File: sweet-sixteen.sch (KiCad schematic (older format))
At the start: 8 parts

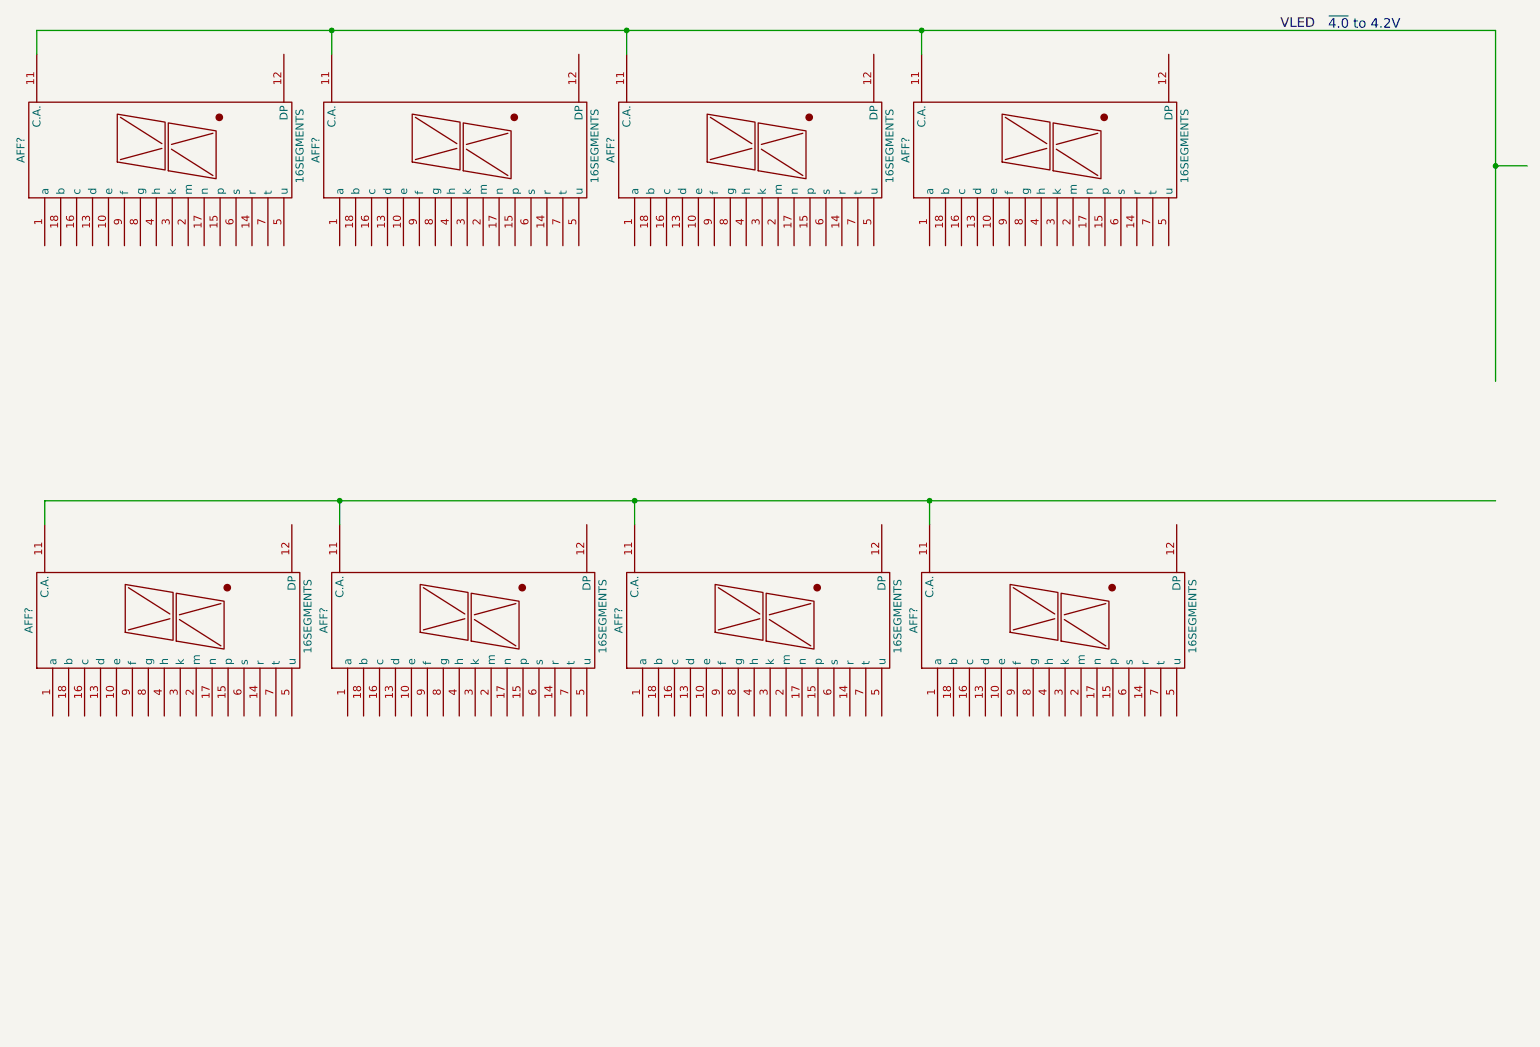
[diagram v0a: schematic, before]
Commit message: add led-drivers to schematic
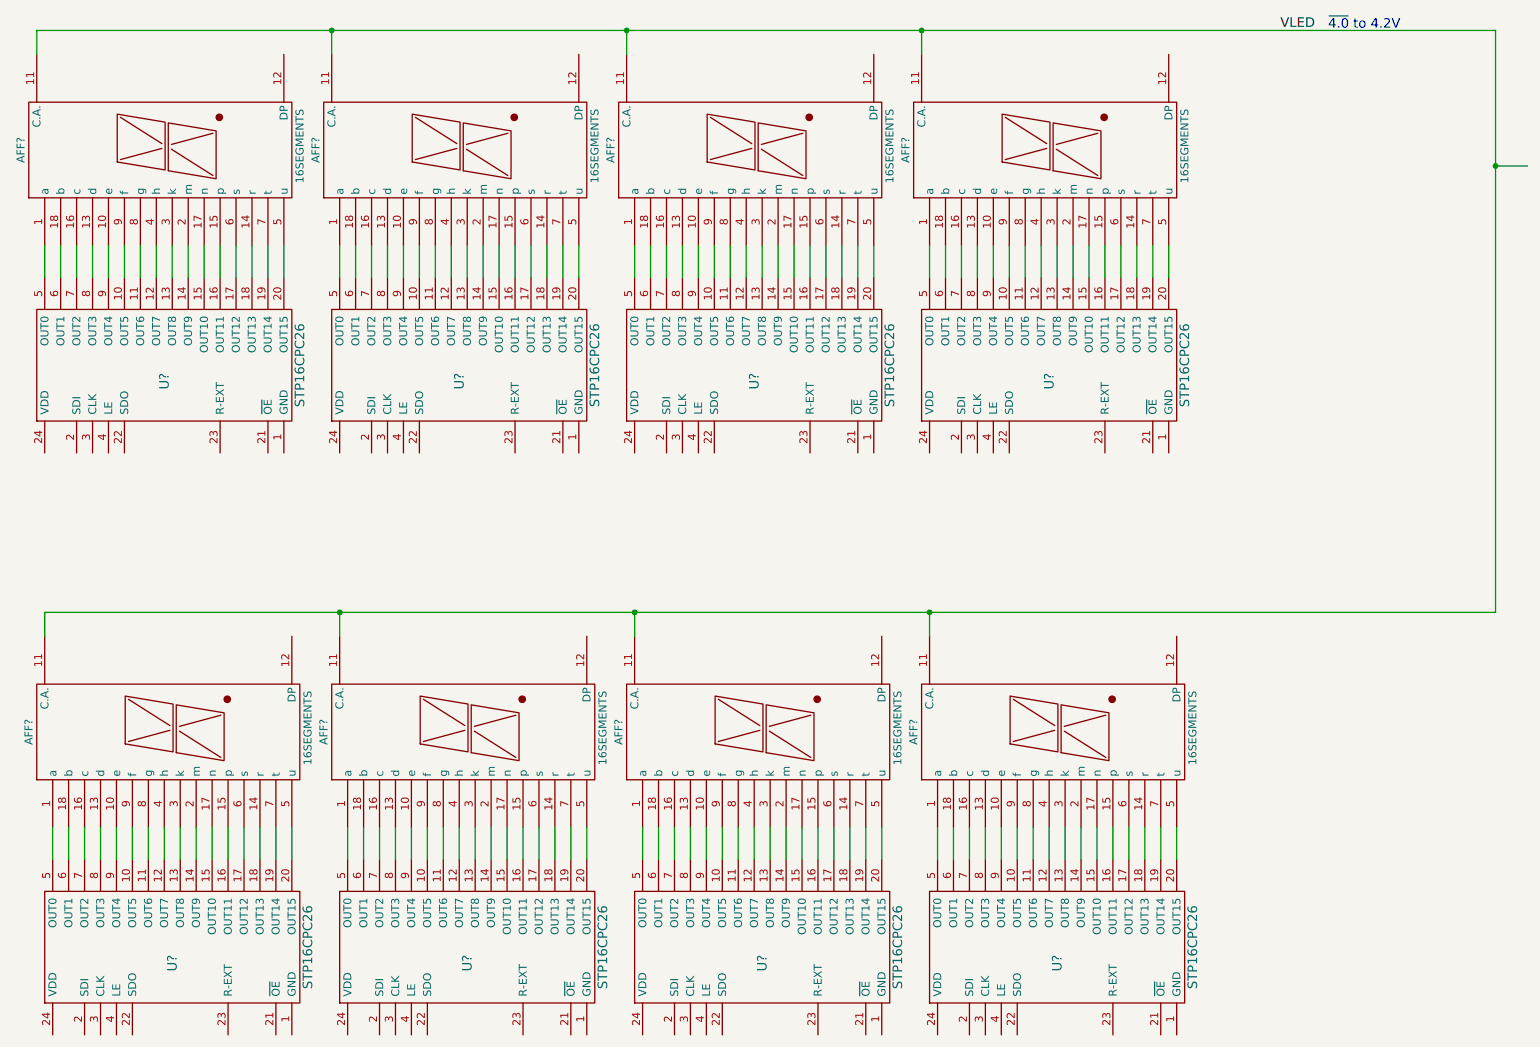
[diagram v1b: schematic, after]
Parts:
- added U? (x8): STP16CPC26, symbol STP16CPC26
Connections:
- wire segments 12 -> 140
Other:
- moved on the sheet: AFF?

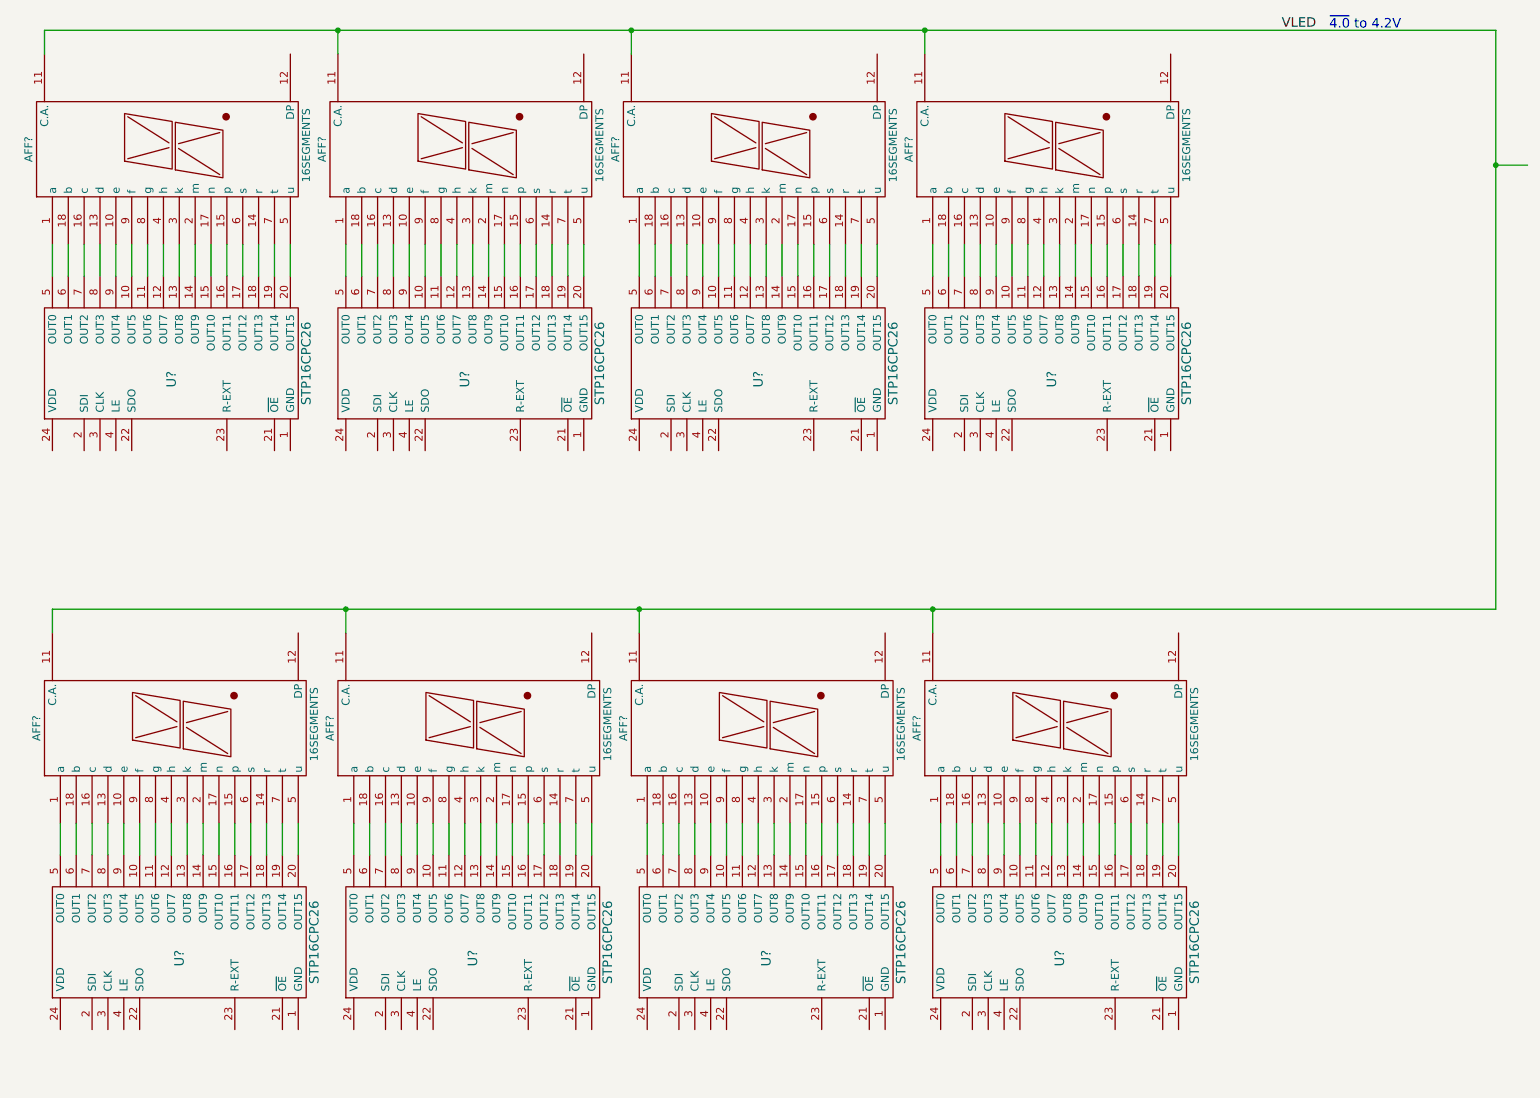
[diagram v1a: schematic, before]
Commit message: wire up displays and driver
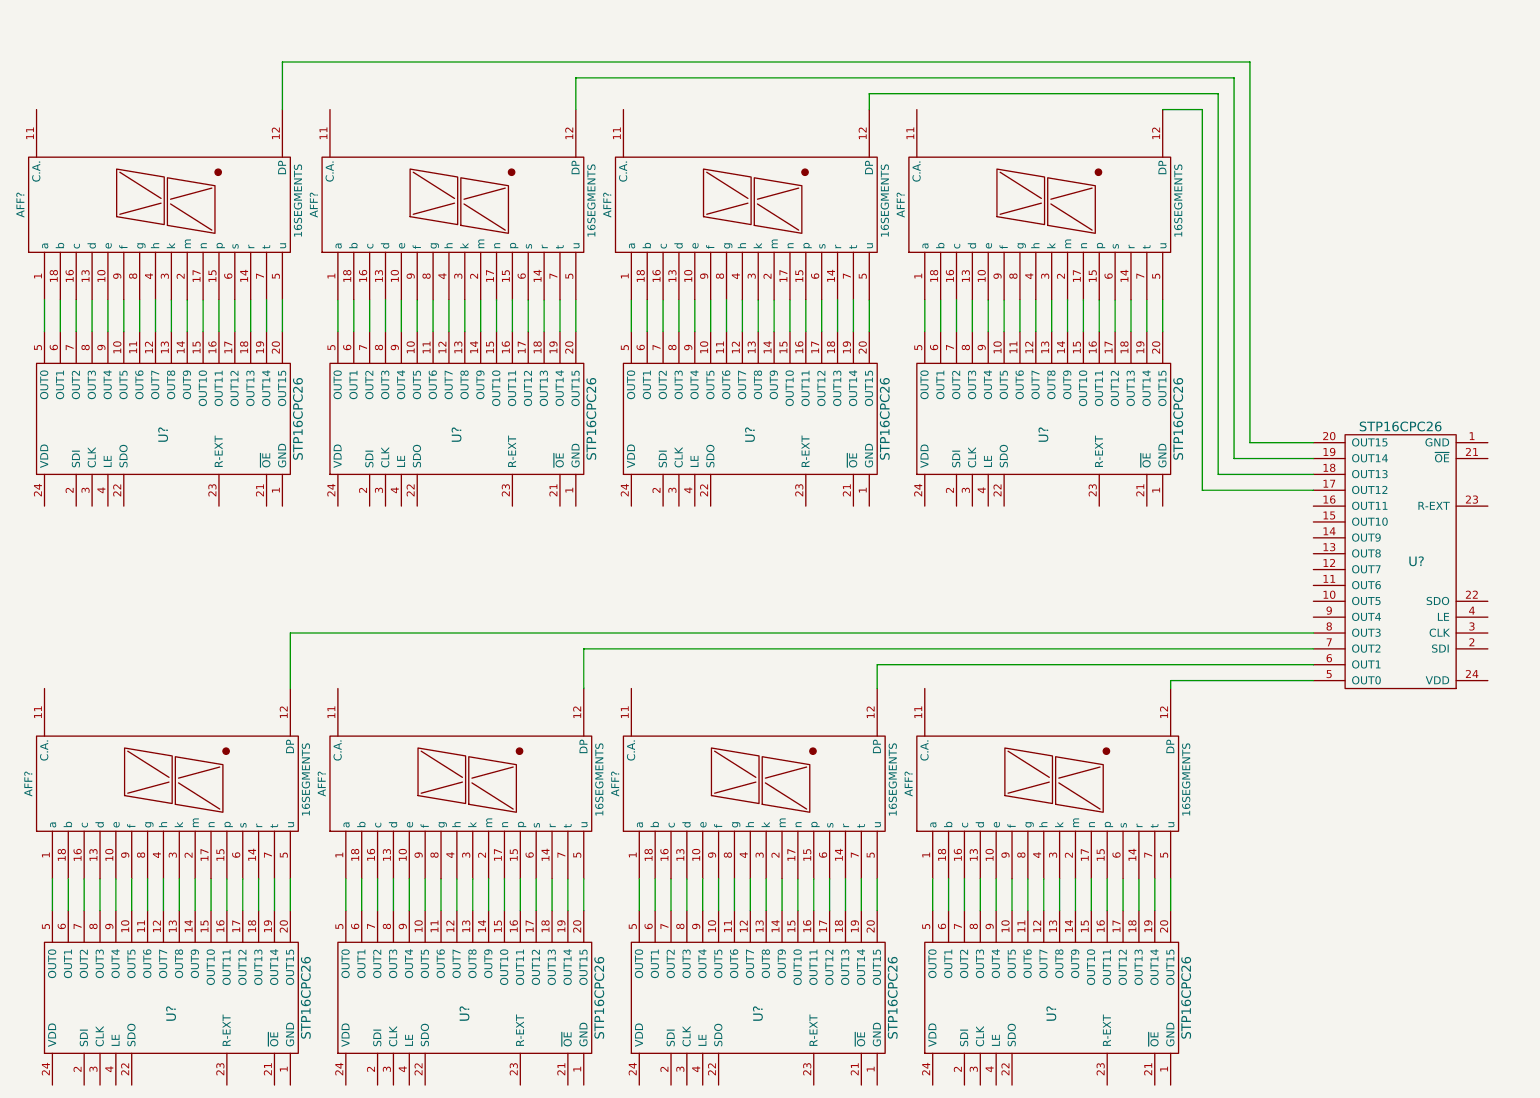
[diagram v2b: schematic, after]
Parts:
- added U?: STP16CPC26, symbol STP16CPC26
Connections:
- net at AFF?.12 (DP): now also U?.20 (OUT15)
- net at AFF?.12 (DP): now also U?.19 (OUT14)
- net at AFF?.12 (DP): now also U?.18 (OUT13)
- net at AFF?.12 (DP): now also U?.17 (OUT12)
- net at AFF?.12 (DP): now also U?.8 (OUT3)
- net at AFF?.12 (DP): now also U?.7 (OUT2)
- net at AFF?.12 (DP): now also U?.6 (OUT1)
- net at AFF?.12 (DP): now also U?.5 (OUT0)
- removed net VLED: AFF?.11 (C.A.), AFF?.11 (C.A.), AFF?.11 (C.A.), AFF?.11 (C.A.), AFF?.11 (C.A.), AFF?.11 (C.A.), AFF?.11 (C.A.), AFF?.11 (C.A.)
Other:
- note removed: "~4.0 to 4.2V"
- moved on the sheet: AFF?, U?

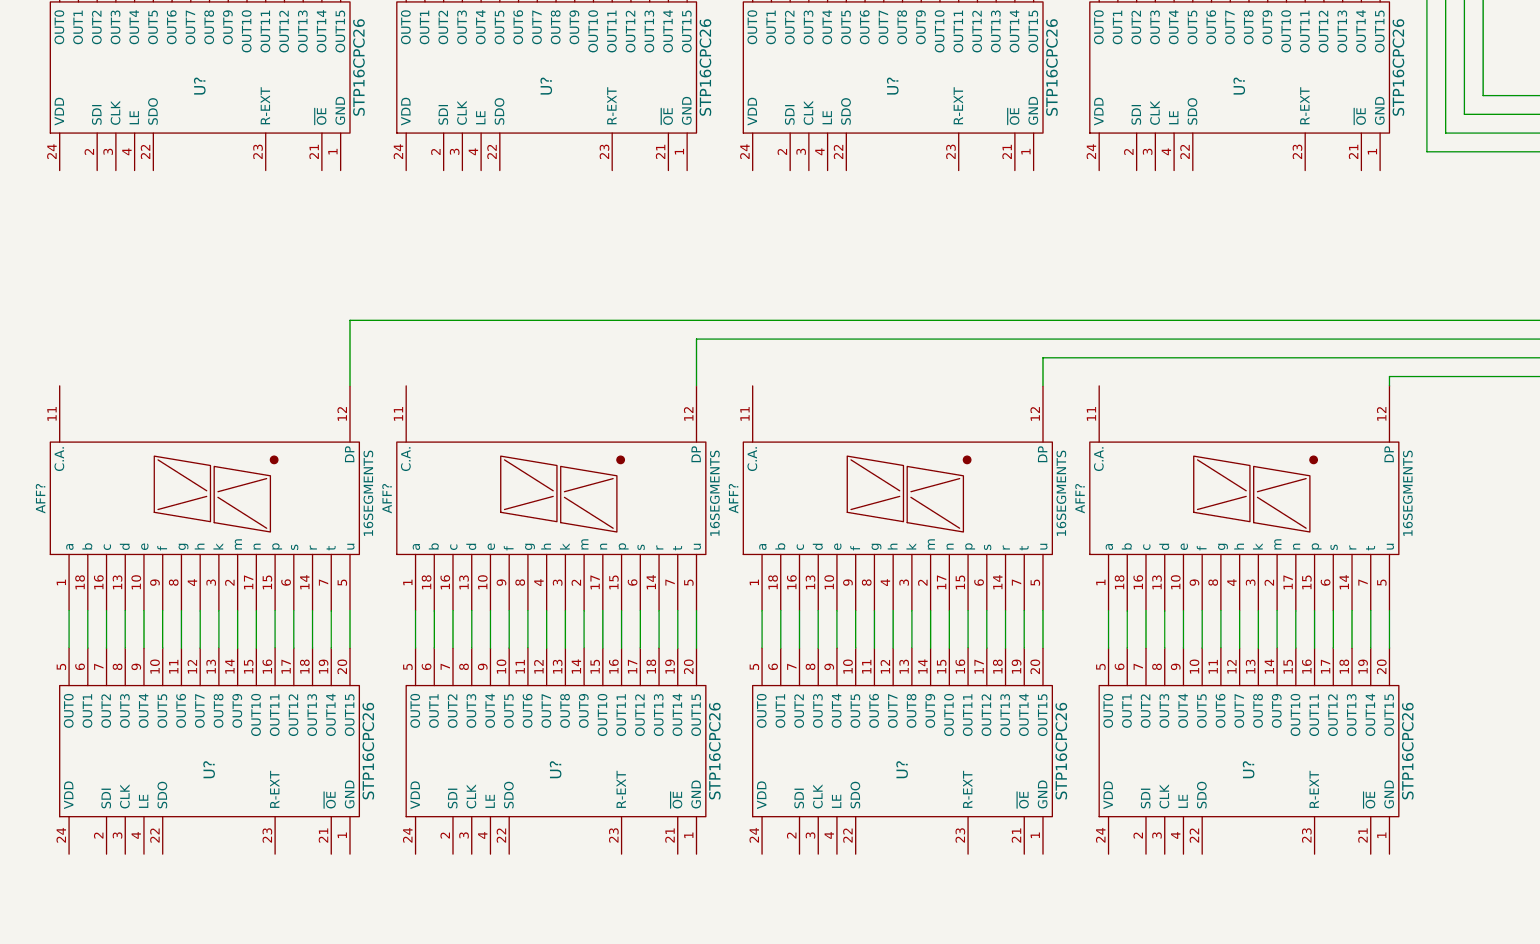
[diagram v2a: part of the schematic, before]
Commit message: add power & gnd
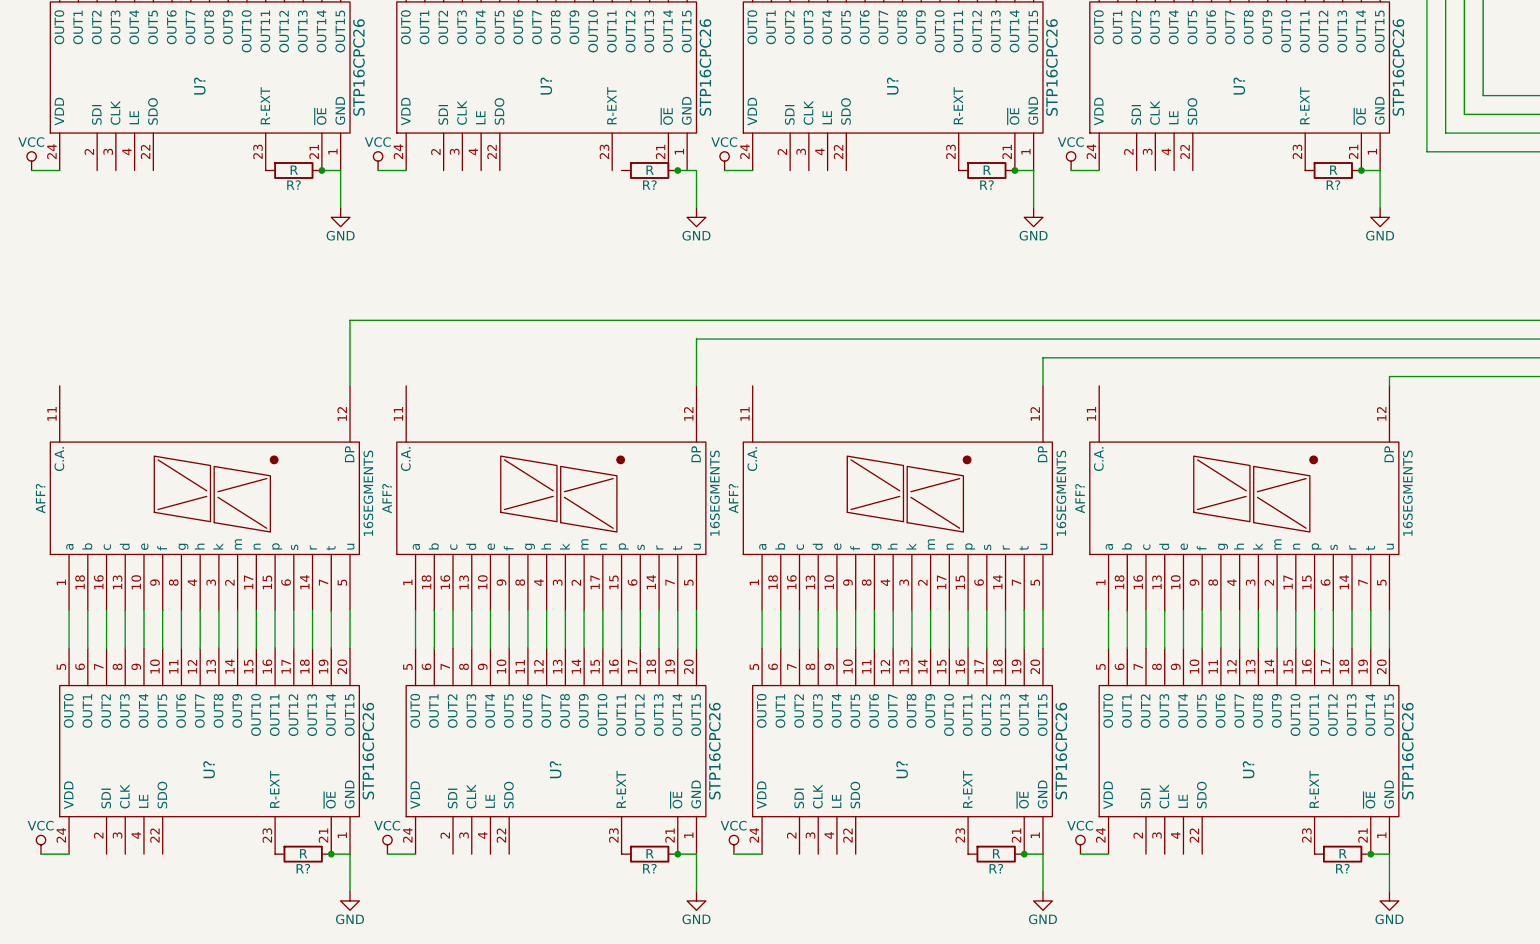
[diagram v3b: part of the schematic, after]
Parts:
- added R? (x8): R, symbol R
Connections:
- net GND: now reaches U?.1 (GND)
- net GND: now also U?.1 (GND), U?.1 (GND), U?.1 (GND), U?.1 (GND), U?.1 (GND), U?.1 (GND), U?.21 (~OE), U?.21 (~OE), U?.21 (~OE), U?.21 (~OE), U?.21 (~OE), U?.21 (~OE), U?.21 (~OE), R?.1, R?.1, R?.1, R?.1, R?.1, R?.1, R?.1, R?.1
- net at U?.23 (R-EXT): now also R?.2 (x7)
- net VCC: now reaches U?.24 (VDD)
- net VCC: now also U?.24 (VDD), U?.24 (VDD), U?.24 (VDD), U?.24 (VDD), U?.24 (VDD), U?.24 (VDD), U?.24 (VDD)

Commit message: restructute sch to be in line, add bus and i/o connector pads
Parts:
- added P?: SDA_I, symbol CONN_01X01
- added P?: CLK_I, symbol CONN_01X01
- added P?: LE_I, symbol CONN_01X01
- added P?: SDA_O, symbol CONN_01X01
- added P?: CLK_O, symbol CONN_01X01
- added P?: LE_O, symbol CONN_01X01
- added P?: VCC_I, symbol CONN_01X01
- added P?: GND_I, symbol CONN_01X01
- added P?: VCC_O, symbol CONN_01X01
- added P?: GND_O, symbol CONN_01X01
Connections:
- net GND: now also P?.1 (P1), P?.1 (P1)
- net VCC: now also P?.1 (P1), P?.1 (P1)
- net at AFF?.12 (DP): no longer U?.20 (OUT15)
- net at AFF?.12 (DP): no longer U?.19 (OUT14)
- net at AFF?.12 (DP): no longer U?.18 (OUT13)
- net at AFF?.12 (DP): no longer U?.17 (OUT12)
- net at AFF?.12 (DP): no longer U?.8 (OUT3)
- net at AFF?.12 (DP): no longer U?.7 (OUT2)
- net at AFF?.12 (DP): no longer U?.6 (OUT1)
- net at AFF?.12 (DP): no longer U?.5 (OUT0)
- net at U?.2 (SDI): now also P?.1 (P1)
- net at U?.22 (SDO): now also U?.2 (SDI) (x4)
- net at U?.3 (CLK): now also U?.3 (CLK), U?.3 (CLK), U?.3 (CLK), U?.3 (CLK), U?.3 (CLK), U?.3 (CLK), U?.3 (CLK), P?.1 (P1), P?.1 (P1)
- net at U?.4 (LE): now also U?.4 (LE), U?.4 (LE), U?.4 (LE), U?.4 (LE), U?.4 (LE), U?.4 (LE), U?.4 (LE), P?.1 (P1), P?.1 (P1)
- net at U?.2 (SDI): now also U?.22 (SDO) (x3)
- net at U?.22 (SDO): now also P?.1 (P1)
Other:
- moved on the sheet: AFF?, R?, U?
